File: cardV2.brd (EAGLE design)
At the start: 84.8 x 53.3 mm, 48 parts, among them IC1 ATTINY1616, IC2 LTC1992-1, IC3 LTC1992, IC4 LTC6911, IC5 LTC2402, SW1 SPST_TACT-EVQQ2, SW2 SPST_TACT-EVQQ2, SW3 SPST_TACT-EVQQ2, SW4 SPST_TACT-EVQQ2

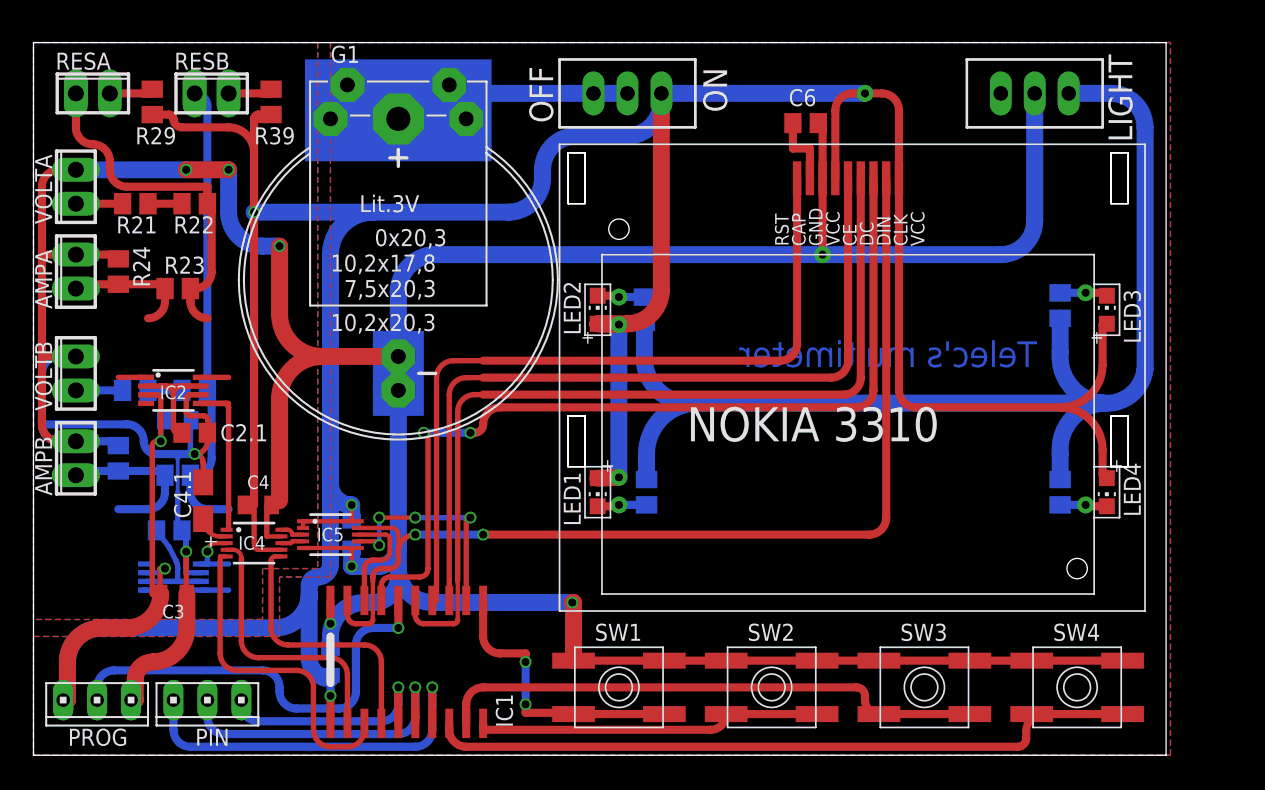
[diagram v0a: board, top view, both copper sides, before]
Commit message: Small changes in board V2 & more test in programming
BTW the programm works, the problem came from the not well connected LCD
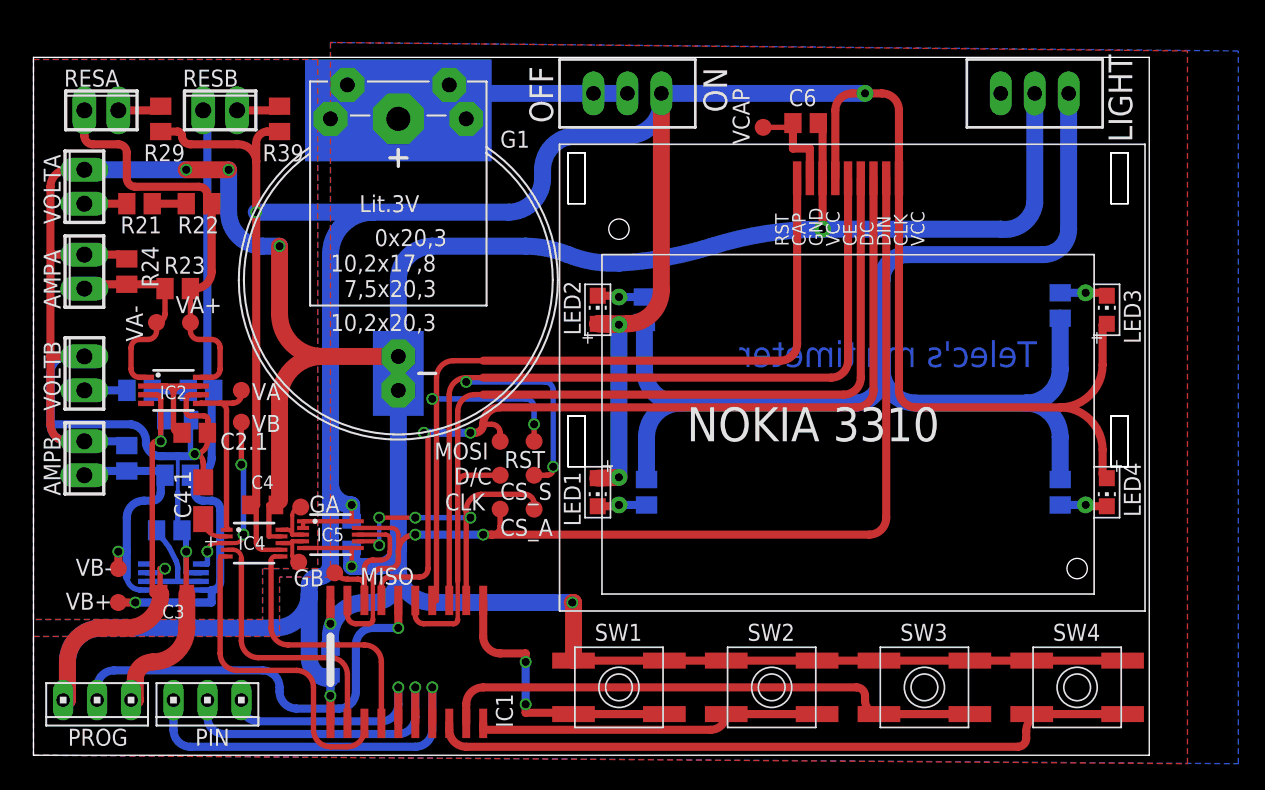
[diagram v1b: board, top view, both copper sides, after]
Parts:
- added CLK, CS_A, CS_S, D/C, GA, GB, MISO, MOSI, RST, VA, VA+, VA-, VB, VB+, VB-, VCAP: TPSQB1,27, testpad:B1,27
- moved R29 1.42 mm to (9.53, 47.6)
- moved RESA 1.42 mm to (5.08, 48.3)
- moved RESB 1.42 mm to (14.0, 48.3)
- moved R39 1.42 mm to (18.4, 47.6)
- moved R24 0.64 mm to (6.99, 36.2)
- moved R34 0.64 mm to (6.99, 22.2)
- moved AMPA 0.64 mm to (3.81, 36.2)
- moved AMPB 0.64 mm to (3.81, 22.2)
- moved VOLTA 0.64 mm to (3.81, 42.5)
- moved VOLTB 0.64 mm to (3.81, 28.6)
- moved R32 0.48 mm to (12.5, 27.3)
- moved R22 0.32 mm to (12.4, 41.3)
- moved R21 0.32 mm to (7.94, 41.3)
- moved R31 0.32 mm to (7.94, 27.3)
- moved C4 0.32 mm to (17.1, 18.7)
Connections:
- net CLK: now also CLK.TP
- net D/C: now also D/C.TP
- net MISO: now also MISO.TP
- net MOSI: now also MOSI.TP
- net N$16: now also VA-.TP
- net N$17: now also VA+.TP
- net N$25: now also VB-.TP
- net N$26: now also VB+.TP
- net N$29: now also GB.TP
- net N$3: now also VCAP.TP
- net N$37: now also GA.TP
- net RAWA: now also VA.TP
- net RAWB: now also VB.TP
- net RST: now also RST.TP
- net _CS_ADC: now also CS_A.TP
- net _CS_SCR: now also CS_S.TP
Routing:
- net _CS_SCR: track 60.0 -> 74.5 mm, vias 0 -> 2
- net RST: track 57.4 -> 68.2 mm, vias 0 -> 2
- net N$26: track 37.2 -> 47.3 mm, vias 0 -> 1
- net RAWB: track 4.71 -> 13.1 mm, vias 1 -> 3
- net _CS_ADC: track 17.3 -> 24.1 mm
- net N$25: track 13.3 -> 19.8 mm, vias 0 -> 1
- net GND: track 323.6 -> 319.2 mm
- net +3V3: track 301.8 -> 297.8 mm
- net D/C: track 66.4 -> 69.8 mm
- net N$16: track 12.5 -> 15.5 mm
- net N$17: track 28.2 -> 31.2 mm
- net MISO: track 8.30 -> 10.8 mm
- net N$3: track 5.39 -> 7.75 mm
- net N$37: track 1.77 -> 4.09 mm
- net MOSI: track 66.5 -> 68.6 mm
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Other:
- board size 84.8 x 53.3 mm -> 83.5 x 52.2 mm

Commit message: Completly separated power lines (analog vs digital)
And more program tests
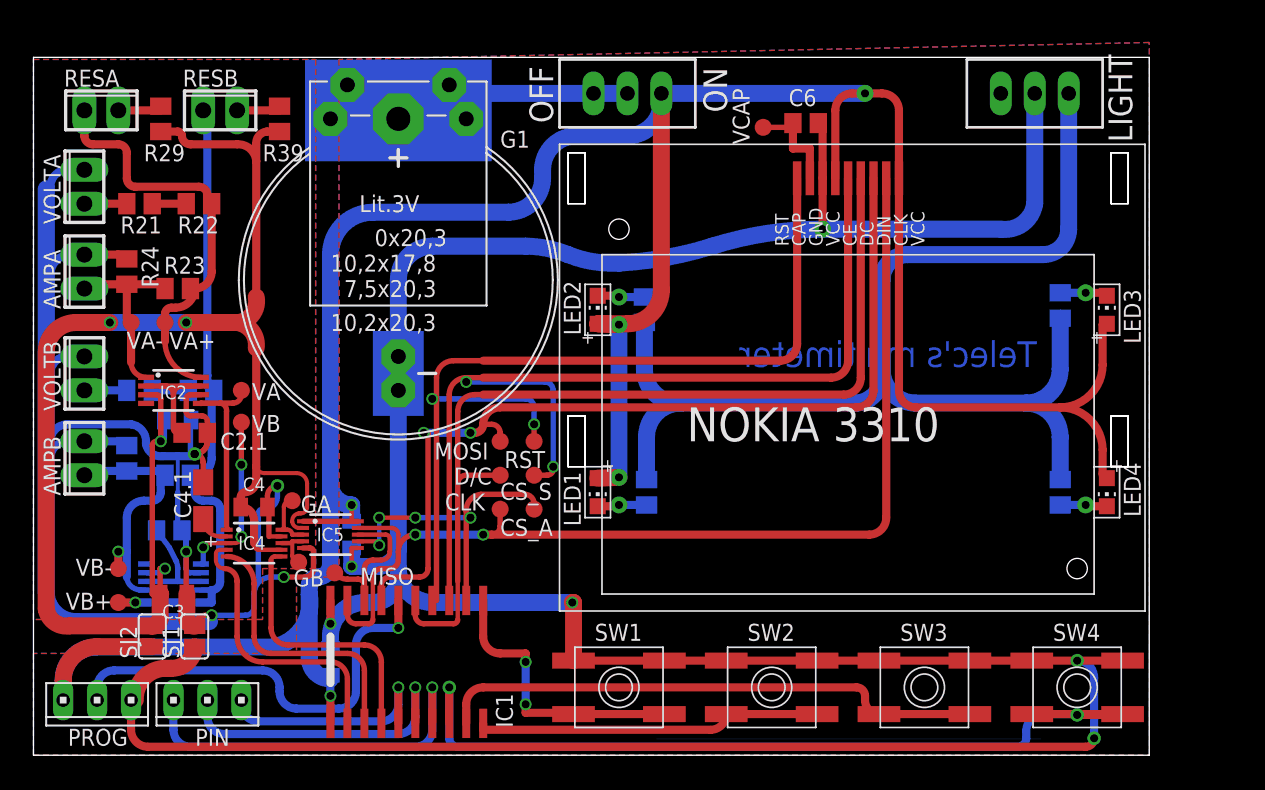
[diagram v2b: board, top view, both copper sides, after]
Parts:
- added SJ1, SJ2: (no value), jumper:SJ
- moved VA+ 1.91 mm to (9.84, 32.4)
- moved VA- 1.90 mm to (7.30, 32.4)
- moved GA 0.79 mm to (19.4, 19.1)
- moved C4 0.65 mm to (16.5, 18.6)
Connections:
- new net AGND: AMPA.2, AMPB.2, C2.1.2, C2.2, C3.1.2, C3.2, C4.1.-, C4.2, IC2.6, IC3.6, IC4.9, IC5.5, R24.2, R34.2, SJ1.2, VOLTA.2, VOLTB.2
- new net V+: C2.1, C3.1, C4.1, IC2.3, IC3.3, IC4.7, IC5.2, R29.2, R39.2, SJ2.2
- net +3V3: now also SJ2.1; no longer C2.1, C3.1, C4.1, IC2.3, IC3.3, IC4.7, IC5.2, R29.2, R39.2
- net GND: now also SJ1.1; no longer AMPA.2, AMPB.2, C2.1.2, C2.2, C3.1.2, C3.2, C4.1.-, C4.2, IC2.6, IC3.6, IC4.9, IC5.5, R24.2, R34.2, VOLTA.2, VOLTB.2
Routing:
- net AGND: track 0.00 -> 160.7 mm, vias 0 -> 6
- net V+: track 0.00 -> 123.3 mm, vias 0 -> 4
- net +3V3: track 297.8 -> 219.2 mm, vias 8 -> 5
- net GND: track 319.2 -> 255.1 mm, vias 9 -> 6
- net SW4: track 53.6 -> 65.3 mm, vias 0 -> 2
- net G1: track 24.3 -> 20.1 mm
- net N$16: track 15.5 -> 14.2 mm
- added copper zone on layer 1, net AGND
- added copper zone on layer 16, net AGND

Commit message: Oops forget to save, see last commit
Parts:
- moved GA 0.65 mm to (19.2, 18.4)
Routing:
- net +3V3: track 219.2 -> 220.3 mm, vias 5 -> 6
- net N$37: track 4.37 -> 3.57 mm
- net AGND: track 160.7 -> 160.3 mm, vias 6 -> 5
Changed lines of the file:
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@@
 <rectangle x1="46.624875" y1="1.171575" x2="75.390375" y2="1.190625" layer="26" rot="R180"/>
 <rectangle x1="46.624875" y1="1.190625" x2="75.390375" y2="1.209675" layer="26" rot="R180"/>
-<rectangle x1="46.624875" y1="1.209675" x2="75.390375" y2="1.228725" layer="16" rot="R180"/>
 <rectangle x1="75.199875" y1="1.228725" x2="75.390375" y2="1.247775" layer="26" rot="R180"/>
 <rectangle x1="46.624875" y1="1.228725" x2="46.815375" y2="1.247775" layer="26" rot="R180"/>
@@
 <element name="IC5" library="HomeMade" package="MSOP10" value="LTC2402" x="22.225" y="16.51" smashed="yes" rot="R270">
 <attribute name="NAME" x="21.19725" y="16.0115" size="1.016" layer="25"/>
-<attribute name="VALUE" x="19.81925" y="19.55575" size="1.016" layer="27"/>
+<attribute name="VALUE" x="20.13675" y="19.397" size="1.016" layer="27"/>
 </element>
 <element name="IC4" library="HomeMade" package="MSOP10" value="LTC6911" x="16.51" y="15.875" smashed="yes" rot="R270">
@@
 <attribute name="NAME" x="16.35125" y="24.1935" size="1.27" layer="25" ratio="10"/>
 </element>
-<element name="GA" library="testpad" package="B1,27" value="TPSQB1,27" x="19.3675" y="19.05" smashed="yes">
-<attribute name="TP_SIGNAL_NAME" value="" x="18.7325" y="17.145" size="1" layer="37"/>
-<attribute name="NAME" x="20.0025" y="18.161" size="1.27" layer="25" ratio="10"/>
+<element name="GA" library="testpad" package="B1,27" value="TPSQB1,27" x="19.20875" y="18.415" smashed="yes">
+<attribute name="TP_SIGNAL_NAME" value="" x="18.57375" y="16.51" size="1" layer="37"/>
+<attribute name="NAME" x="19.939" y="19.05" size="1.27" layer="25" ratio="10" rot="R90"/>
 </element>
 <element name="GB" library="testpad" package="B1,27" value="TPSQB1,27" x="19.84375" y="14.44625" smashed="yes">
@@
 <vertex x="83.5025" y="53.34"/>
 <vertex x="22.86" y="52.07"/>
-<vertex x="22.86" y="13.335"/>
-<vertex x="19.685" y="13.335"/>
+<vertex x="22.86" y="13.0175"/>
+<vertex x="19.685" y="13.0175"/>
 <vertex x="19.685" y="7.62"/>
 </polygon>
@@
 <vertex x="83.5025" y="53.34"/>
 <vertex x="22.86" y="52.07"/>
-<vertex x="22.86" y="13.335"/>
-<vertex x="19.685" y="13.335"/>
+<vertex x="22.86" y="13.0175"/>
+<vertex x="19.685" y="13.0175"/>
 <vertex x="19.685" y="7.62"/>
 <vertex x="0" y="7.62"/>
@@
 <wire x1="2.2225" y1="5.588" x2="2.2225" y2="4.1275" width="1.27" layer="1"/>
 <contactref element="IC5" pad="10"/>
-<wire x1="20.175" y1="17.51" x2="23.8125" y2="17.51" width="0.4064" layer="1"/>
-<wire x1="24.275" y1="17.51" x2="23.8125" y2="17.51" width="0.4064" layer="1"/>
+<wire x1="24.275" y1="17.51" x2="23.8125" y2="17.51" width="0.3048" layer="1"/>
+<via x="20.47875" y="18.7325" extent="1-16" drill="0.6" shape="square"/>
+<wire x1="20.47875" y1="18.7325" x2="23.8125" y2="18.7325" width="0.3048" layer="16"/>
+<wire x1="20.175" y1="17.51" x2="20.175" y2="18.42875" width="0.3048" layer="1"/>
+<wire x1="20.175" y1="18.42875" x2="20.47875" y2="18.7325" width="0.3048" layer="1" curve="-90"/>
 </signal>
 <signal name="N$2">
@@
 <contactref element="IC4" pad="10"/>
 <wire x1="18.56" y1="16.875" x2="19.0025" y2="16.875" width="0.3302" layer="1"/>
-<wire x1="19.0025" y1="16.875" x2="19.3675" y2="16.51" width="0.3302" layer="1" curve="-90"/>
-<wire x1="19.3675" y1="16.51" x2="20.175" y2="16.51" width="0.3302" layer="1"/>
+<wire x1="19.0025" y1="16.875" x2="19.3675" y2="16.51" width="0.3048" layer="1" curve="-90"/>
+<wire x1="19.3675" y1="16.51" x2="20.175" y2="16.51" width="0.3048" layer="1"/>
 <contactref element="GA" pad="TP"/>
-<wire x1="19.3675" y1="19.05" x2="19.20875" y2="19.05" width="0.3048" layer="1"/>
-<wire x1="19.20875" y1="19.05" x2="18.7325" y2="18.57375" width="0.3048" layer="1" curve="90"/>
-<wire x1="18.7325" y1="18.57375" x2="18.7325" y2="17.0475" width="0.3048" layer="1"/>
+<wire x1="19.20875" y1="18.415" x2="18.89125" y2="18.0975" width="0.3048" layer="1"/>
+<wire x1="18.89125" y1="18.0975" x2="18.7325" y2="17.93875" width="0.3048" layer="1" curve="90"/>
+<wire x1="18.7325" y1="17.93875" x2="18.7325" y2="17.0475" width="0.3048" layer="1"/>
 <wire x1="18.7325" y1="17.0475" x2="18.56" y2="16.875" width="0.3048" layer="1" curve="-90"/>
 </signal>
@@
 <wire x1="17.78" y1="7.62" x2="16.51" y2="8.89" width="0.4064" layer="1" curve="-90"/>
 <wire x1="16.51" y1="8.89" x2="16.51" y2="12.825" width="0.4064" layer="1"/>
-<wire x1="16.51" y1="12.825" x2="14.46" y2="14.875" width="0.4064" layer="1" curve="90"/>
+<wire x1="16.51" y1="12.825" x2="14.46" y2="14.875" width="0.3048" layer="1" curve="90"/>
 </signal>
 <signal name="G2">
@@
 <wire x1="8.41375" y1="23.33625" x2="7.3025" y2="24.765" width="0.6096" layer="16" curve="90"/>
 <wire x1="10.795" y1="22.38375" x2="12.065" y2="22.38375" width="0.6096" layer="16"/>
-<wire x1="12.065" y1="22.38375" x2="12.0625" y2="22.5425" width="0.6096" layer="16"/>
-<wire x1="11.7475" y1="22.5425" x2="12.0625" y2="22.5425" width="0.4064" layer="16"/>
-<via x="12.0625" y="22.5425" extent="1-16" drill="0.6" shape="square"/>
 <wire x1="12.0625" y1="22.5425" x2="12.065" y2="22.5425" width="0.4064" layer="1" curve="0.150186"/>
 <wire x1="12.065" y1="22.5425" x2="13.01624375" y2="23.498175" width="0.4064" layer="1" curve="89.965645"/>
@@
 <wire x1="11.4775" y1="10.2395" x2="11.4775" y2="12.065" width="1.27" layer="1"/>
 <wire x1="2.54" y1="43.815" x2="3.81" y2="43.815" width="0.6096" layer="16"/>
-<wire x1="20.175" y1="15.51" x2="20.685" y2="15.51" width="0.4064" layer="1"/>
-<wire x1="20.685" y1="15.51" x2="20.955" y2="15.24" width="0.4064" layer="1" curve="-90"/>
+<wire x1="20.175" y1="15.51" x2="20.685" y2="15.51" width="0.3048" layer="1"/>
+<wire x1="20.685" y1="15.51" x2="20.955" y2="15.24" width="0.3048" layer="1" curve="-90"/>
 <wire x1="20.955" y1="15.24" x2="20.955" y2="13.97" width="0.4064" layer="1"/>
 <wire x1="20.955" y1="13.97" x2="20.32" y2="13.335" width="0.4064" layer="1" curve="-90"/>
@@
 <wire x1="16.51" y1="12.065" x2="16.51" y2="11.1125" width="0.4064" layer="16"/>
 <wire x1="16.51" y1="11.1125" x2="15.875" y2="10.4775" width="0.4064" layer="16" curve="-90"/>
-<wire x1="15.875" y1="10.4775" x2="13.335" y2="10.4775" width="0.4064" layer="16"/>
-<wire x1="13.335" y1="10.4775" x2="12.8905" y2="10.4775" width="0.4064" layer="1"/>
+<wire x1="15.875" y1="10.4775" x2="13.6525" y2="10.4775" width="0.4064" layer="16"/>
+<wire x1="13.6525" y1="10.4775" x2="12.8905" y2="10.4775" width="0.4064" layer="1"/>
 <wire x1="12.8905" y1="10.4775" x2="12.065" y2="9.652" width="0.4064" layer="1" curve="90"/>
-<via x="13.335" y="10.4775" extent="1-16" drill="0.6" shape="square"/>
+<via x="13.6525" y="10.4775" extent="1-16" drill="0.6" shape="square"/>
 <via x="18.7325" y="13.335" extent="1-16" drill="0.6" shape="square"/>
 <wire x1="3.81" y1="29.845" x2="2.54" y2="29.845" width="0.6096" layer="16"/>
@@
 <wire x1="7.3025" y1="24.765" x2="2.54" y2="24.765" width="0.6096" layer="16"/>
 <wire x1="2.54" y1="24.765" x2="1.27" y2="23.495" width="0.6096" layer="16" curve="90"/>
-<wire x1="13.335" y1="10.4775" x2="13.335" y2="9.8425" width="0.6096" layer="16"/>
+<wire x1="13.6525" y1="10.4775" x2="13.335" y2="9.8425" width="0.6096" layer="16"/>
 <polygon width="0.4064" layer="16" isolate="0.4064">
 <vertex x="0" y="52.07"/>
@@
 <wire x1="13.015" y1="24.9733125" x2="13.015" y2="24.13" width="0.4064" layer="1"/>
 <wire x1="11.7475" y1="25.035" x2="11.7475" y2="22.5425" width="0.4064" layer="16"/>
-<wire x1="12.0625" y1="22.5425" x2="12.065" y2="22.5425" width="0.4064" layer="16"/>
 <via x="12.065" y="22.5425" extent="1-16" drill="0.6" diameter="1.016" shape="square"/>
 <wire x1="12.065" y1="22.5425" x2="13.015" y2="23.4925" width="0.4064" layer="1" curve="90"/>
@@
 <wire x1="3.175" y1="10.00125" x2="0.9525" y2="12.22375" width="1.27" layer="16" curve="-90"/>
 <wire x1="0.9525" y1="12.22375" x2="0.9525" y2="42.38625" width="1.27" layer="16"/>
-<wire x1="13.335" y1="9.8425" x2="13.17625" y2="10.00125" width="0" layer="19" extent="16-16"/>
 </signal>
 <signal name="V+">
@@
 <wire x1="17.465" y1="46.675" x2="18.415" y2="46.675" width="0.6096" layer="1"/>
 <wire x1="20.175" y1="17.01" x2="19.97875" y2="17.01" width="0.3048" layer="1"/>
-<wire x1="19.97875" y1="17.01" x2="19.3675" y2="17.4625" width="0.3048" layer="1" curve="-90"/>
-<wire x1="19.3675" y1="17.4625" x2="19.84375" y2="18.0975" width="0.3048" layer="1" curve="-90"/>
-<wire x1="19.84375" y1="18.0975" x2="20.0025" y2="18.0975" width="0.3048" layer="1"/>
-<wire x1="20.0025" y1="18.0975" x2="20.47875" y2="18.57375" width="0.3048" layer="1" curve="90"/>
-<wire x1="20.47875" y1="18.57375" x2="20.47875" y2="20.32" width="0.3048" layer="1"/>
-<wire x1="20.47875" y1="20.32" x2="19.685" y2="21.11375" width="0.3048" layer="1" curve="90"/>
 <wire x1="16.66875" y1="20.6375" x2="15.875" y2="19.685" width="0.6096" layer="1" curve="-90"/>
 <wire x1="15.875" y1="19.685" x2="15.51" y2="19.32" width="0.6096" layer="1" curve="90"/>
@@
 <wire x1="9.795" y1="23.765" x2="9.525" y2="23.495" width="0.4064" layer="16" curve="-90"/>
 <wire x1="8.89" y1="9.68375" x2="8.89" y2="9.652" width="0.4064" layer="1"/>
+<wire x1="20.175" y1="17.01" x2="20.82" y2="17.01" width="0.3048" layer="1"/>
+<wire x1="20.82" y1="17.01" x2="21.2725" y2="17.4625" width="0.3048" layer="1" curve="90"/>
+<wire x1="21.2725" y1="17.4625" x2="21.2725" y2="19.52625" width="0.3048" layer="1"/>
+<wire x1="21.2725" y1="19.52625" x2="19.685" y2="21.11375" width="0.3048" layer="1" curve="90"/>
 </signal>
 </signals>
